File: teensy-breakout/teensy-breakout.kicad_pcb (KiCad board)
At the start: 6 copper layers, 240.5 x 168.5 mm, 82 parts, among them J1 USB_B, J10 1988820, J11 1988817, J12 1988817, J13 1988817, J14 1988817, J15 1988820, J17 1988956, J18 1988817, J19 1989010, J2 1988820, J20 1989010, J21 1988956, J22 1988817, J3 1988820, J4 1988820, J5 1988820, J6 1988820, J7 1988820, J8 1988833, J9 1988956, Q1 IRL530NSTRLPBF, SW1 7101MD9AQE, U1 Teensy4.1, U10 LSF0102DCUR, U3 FT232RL, U6 ICL7667CBAZA-TDKR, U7 LSF0102DCUR, U8 LSF0102DCUR

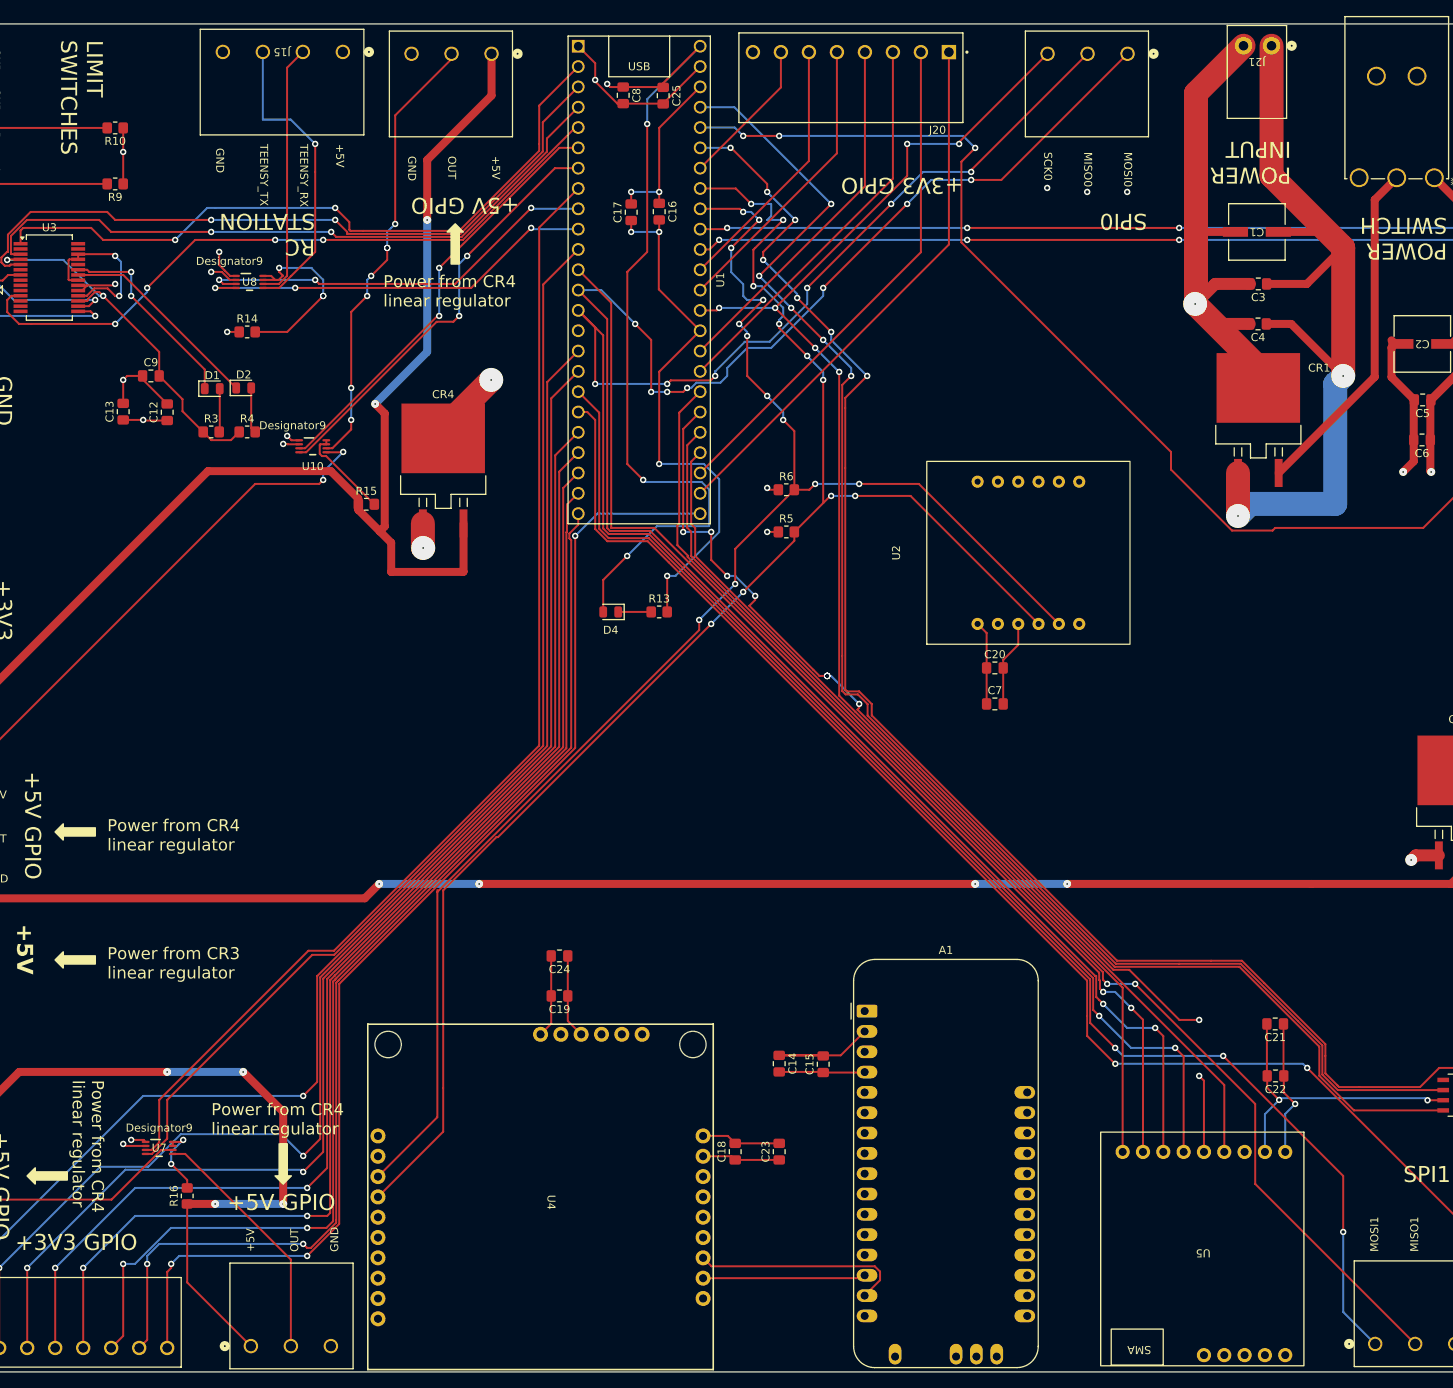
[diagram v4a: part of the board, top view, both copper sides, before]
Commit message: Added connection for limit switches, started work on adding headers
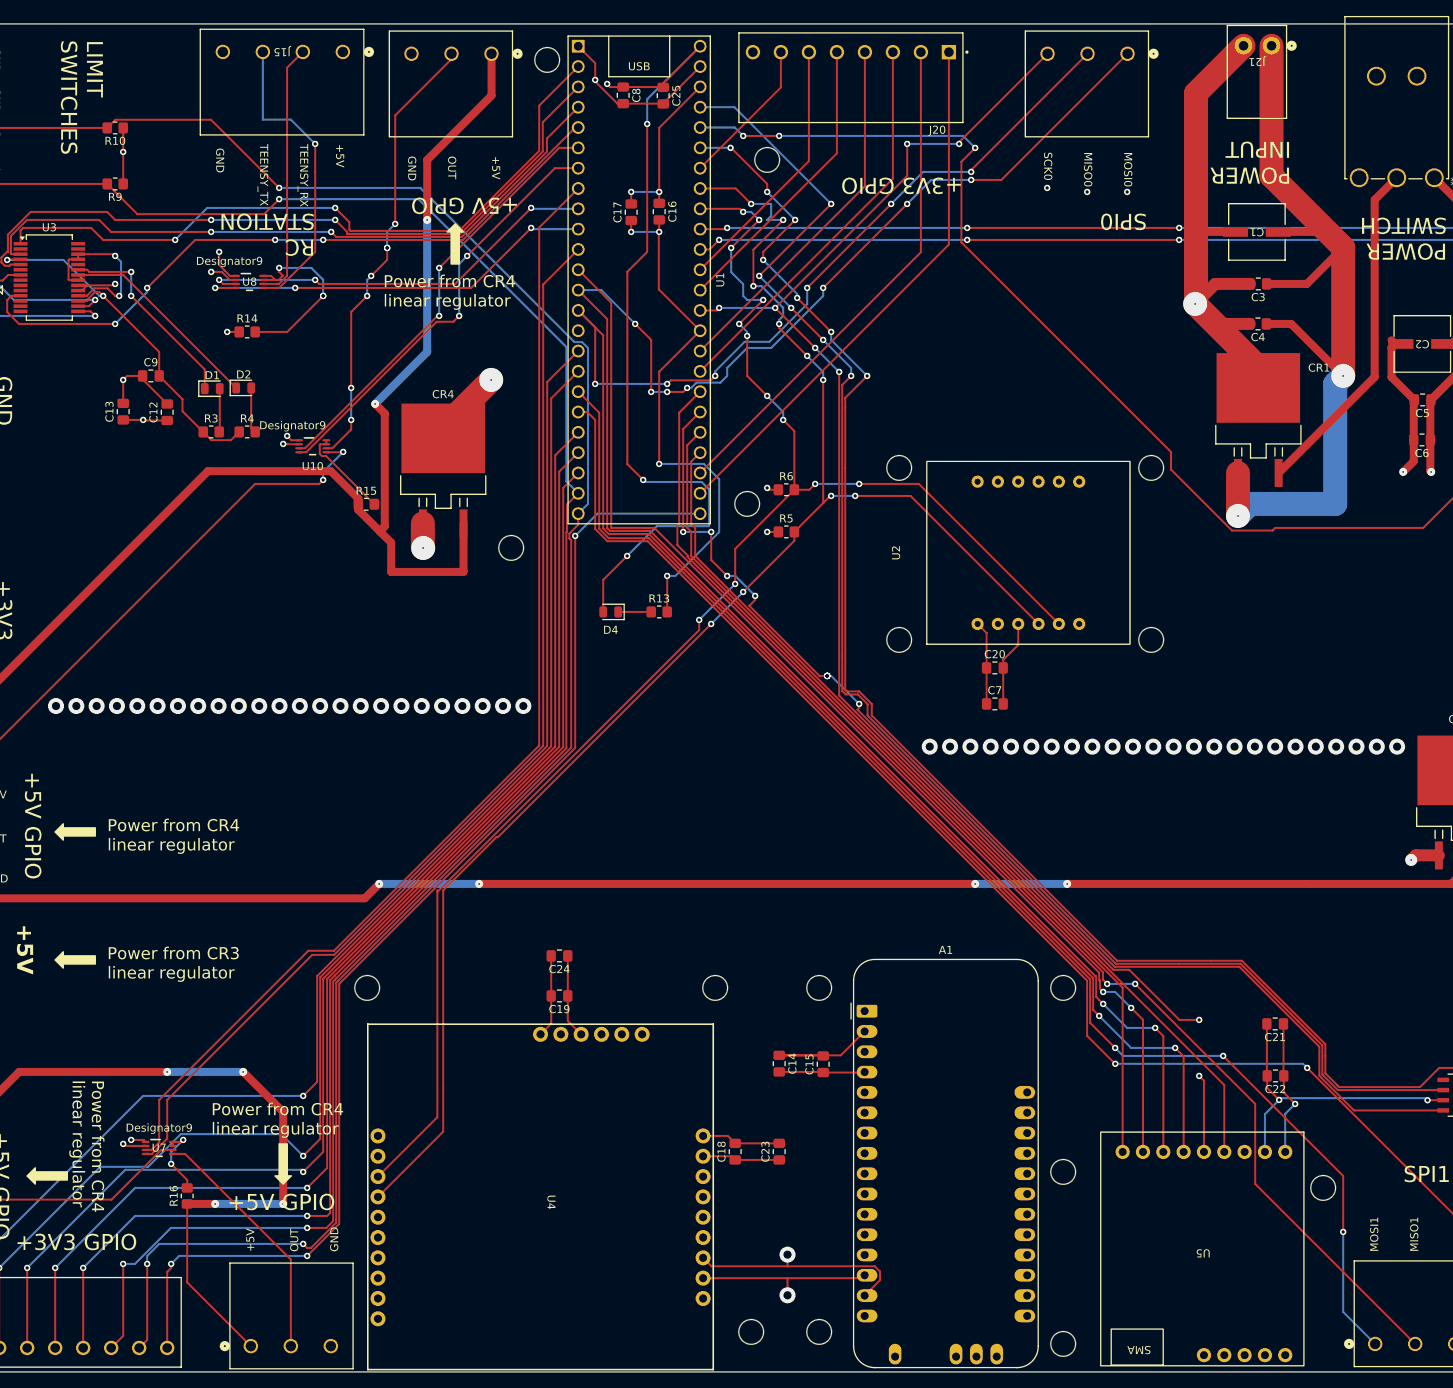
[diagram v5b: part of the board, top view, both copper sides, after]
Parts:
- added ?: , clipboard:fe42560d-e869-41d1-821b-38ac966b38b9, F.Cu at (164.0, 147.0)
- added ?: , clipboard:fe42560d-e869-41d1-821b-38ac966b38b9, F.Cu at (124.5, 86.5)
- added ?: , clipboard:fe42560d-e869-41d1-821b-38ac966b38b9, F.Cu at (133.5, 190.0)
- added ?: , clipboard:fe42560d-e869-41d1-821b-38ac966b38b9, F.Cu at (133.5, 147.0)
- added ?: , clipboard:fe42560d-e869-41d1-821b-38ac966b38b9, F.Cu at (99.5, 31.0)
- added ?: , clipboard:fe42560d-e869-41d1-821b-38ac966b38b9, F.Cu at (125.0, 190.0)
- added ?: , clipboard:fe42560d-e869-41d1-821b-38ac966b38b9, F.Cu at (164.0, 191.5)
- added ?: , clipboard:fe42560d-e869-41d1-821b-38ac966b38b9, F.Cu at (77.0, 147.0)
- added ?: , clipboard:fe42560d-e869-41d1-821b-38ac966b38b9, F.Cu at (143.5, 103.5)
- added ?: , clipboard:fe42560d-e869-41d1-821b-38ac966b38b9, F.Cu at (143.5, 82.0)
- added ?: , clipboard:fe42560d-e869-41d1-821b-38ac966b38b9, F.Cu at (175.0, 103.5)
- added ?: , clipboard:fe42560d-e869-41d1-821b-38ac966b38b9, F.Cu at (196.5, 172.0)
- added ?: , clipboard:fe42560d-e869-41d1-821b-38ac966b38b9, F.Cu at (164.0, 170.0)
- added ?: , clipboard:fe42560d-e869-41d1-821b-38ac966b38b9, F.Cu at (95.0, 92.0)
- added ?: , clipboard:fe42560d-e869-41d1-821b-38ac966b38b9, F.Cu at (175.0, 82.0)
- added ?: , clipboard:fe42560d-e869-41d1-821b-38ac966b38b9, F.Cu at (120.5, 147.0)
- added ?: , clipboard:fe42560d-e869-41d1-821b-38ac966b38b9, F.Cu at (127.0, 43.5)
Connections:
- J9 pad 1: GND -> Net-(D3-K)
- J9 pad 2: led_pos -> +12V
- R8 pad 2: led_pos -> Net-(D3-A)
- U1 pad 23: /J0_6 -> /LIM_L
- U1 pad 24: /J0_7 -> /LIM_R
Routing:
- net GND: track 338.7 -> 657.4 mm, vias 18 -> 21
- net +3V3: track 166.8 -> 345.5 mm, vias 11 -> 13
- net +5V: track 178.8 -> 309.3 mm, vias 9 -> 10
- net /PUL: track 190.0 -> 307.1 mm, vias 5 -> 6
- net /BRAKE: track 138.5 -> 252.3 mm, vias 3 -> 4
- net /ALM: track 228.3 -> 340.0 mm, vias 7 -> 8
- net /UART1 RX: track 87.4 -> 196.0 mm, vias 2 -> 3
- net /J1_7: track 18.7 -> 126.7 mm, vias 0 -> 1
- net /I2C0_SCL: track 199.3 -> 305.6 mm, vias 10 -> 11
- net /UART1 TX: track 90.0 -> 196.3 mm, vias 2 -> 3
- net /UART1 RTS: track 83.7 -> 186.8 mm, vias 2 -> 3
- net /I2C0_SDA: track 198.3 -> 300.4 mm, vias 12 -> 13
- net /UART1 CTS: track 85.8 -> 185.8 mm, vias 4 -> 5
- net Net-(U1-17_A3_TX4_SDA1): track 141.0 -> 238.0 mm, vias 4 -> 5
- net Net-(U1-16_A2_RX4_SCL1): track 148.5 -> 242.8 mm, vias 4 -> 5
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
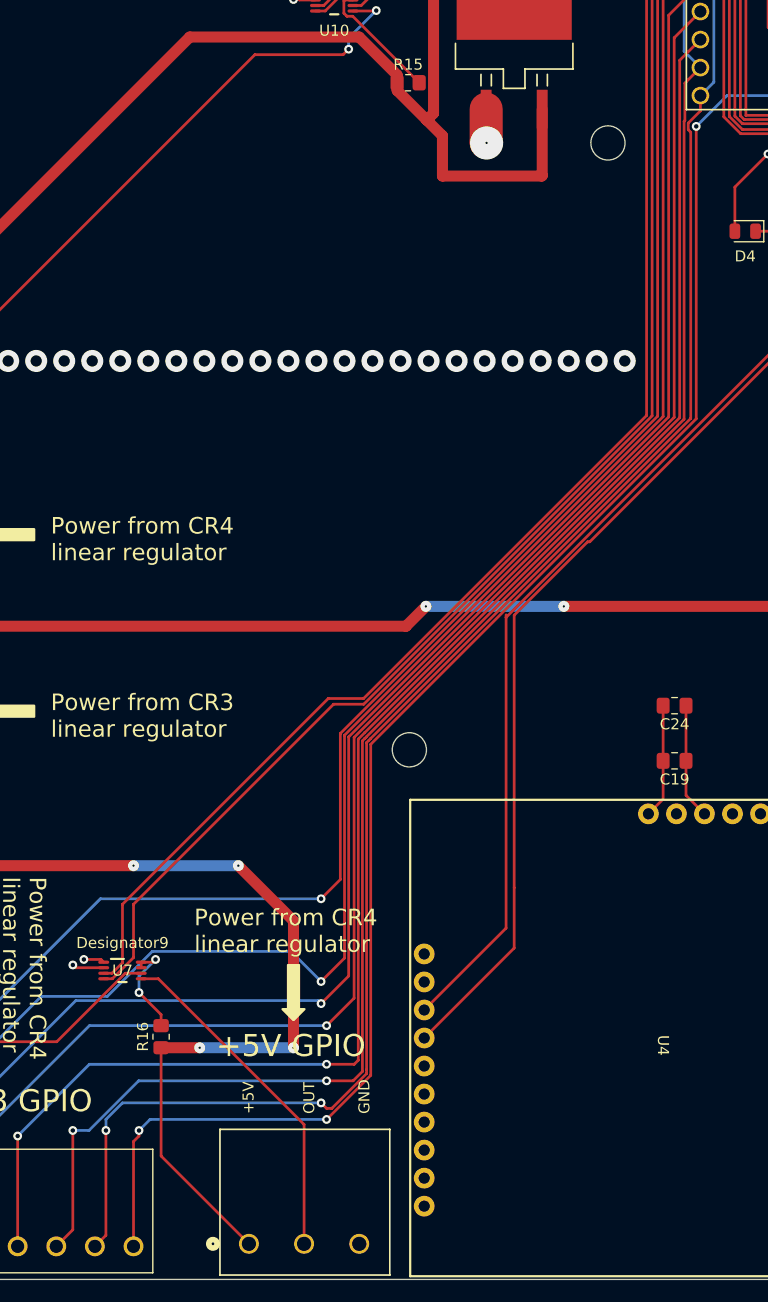
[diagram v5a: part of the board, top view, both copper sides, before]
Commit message: Fixed limit switch connection
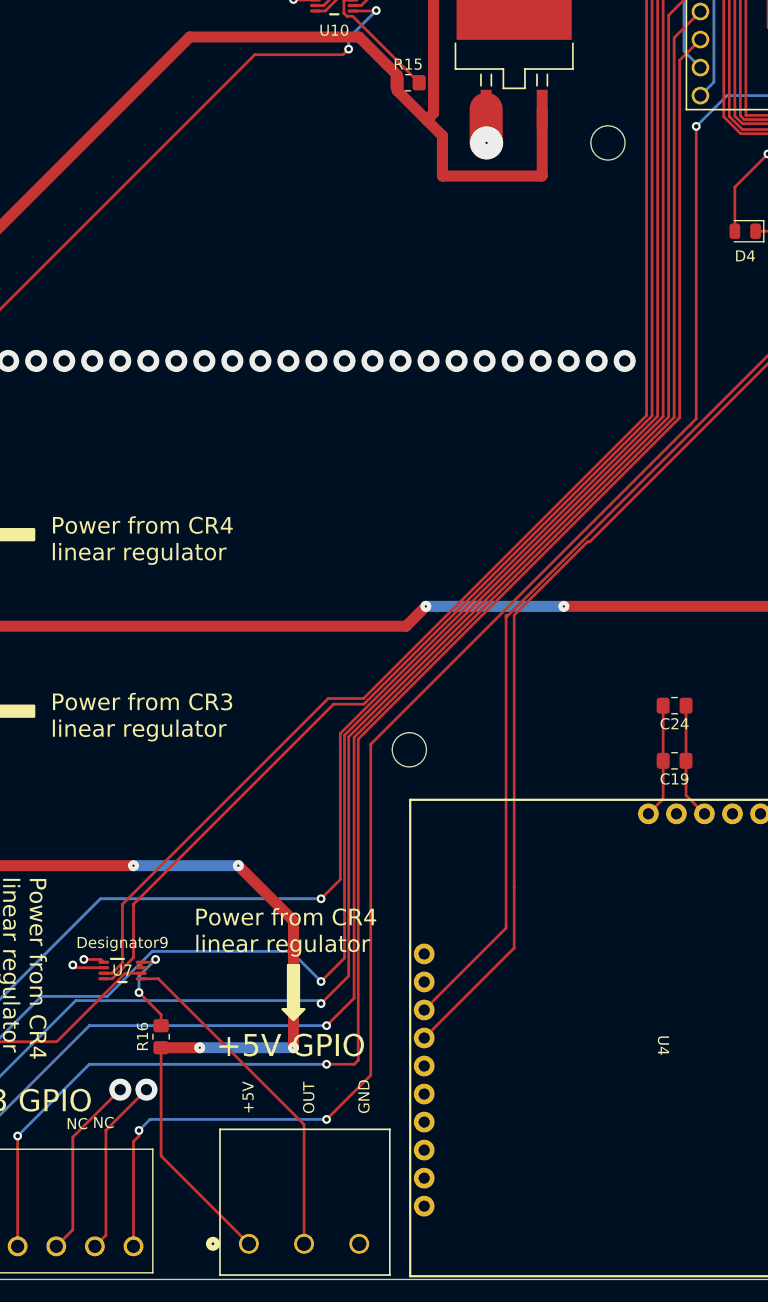
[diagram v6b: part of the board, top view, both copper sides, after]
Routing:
- net /J0_6: track 173.7 -> 16.6 mm, vias 3 -> 1
- net /J0_7: track 165.9 -> 16.1 mm, vias 3 -> 1
- net /LIM_L: track 114.5 -> 145.0 mm, vias 1 -> 2
- net /LIM_R: track 121.7 -> 148.6 mm, vias 1 -> 2
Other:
- board text added: "NC"

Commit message: Final commit before meeting
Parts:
- added REF**: PinHeader_1x06_P2.54mm_Vertical, Connector_PinHeader_2.54mm:PinHeader_1x06_P2.54mm_Vertical, F.Cu at (171.4, 140.7)
- added REF**: PinHeader_1x02_P2.54mm_Vertical, Connector_PinHeader_2.54mm:PinHeader_1x02_P2.54mm_Vertical, F.Cu at (144.3, 72.7)
- moved ? 163.6 mm to (196.5, 191.6)
- moved SW1 1.17 mm to (210.4, 46.9)
- moved J9 0.50 mm to (250.8, 44.1)
- moved J6 0.48 mm to (250.8, 78.8)
- moved J2 0.43 mm to (250.8, 55.7)
- moved J4 0.37 mm to (250.9, 103.7)
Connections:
- J9 pad 2: +12V -> Net-(D3-A)
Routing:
- net GND: track 657.4 -> 737.3 mm, vias 21 -> 22
- net Net-(D3-K): track 79.7 -> 123.9 mm, vias 0 -> 4
- net /RF_G0: track 171.5 -> 199.0 mm
- net /RF_RST: track 171.6 -> 198.4 mm
- net /RF_CS: track 214.2 -> 241.0 mm
- net /MOSI0: track 307.2 -> 334.0 mm
- net /MISO0: track 295.9 -> 322.7 mm
- net Net-(D3-A): track 5.89 -> 27.7 mm
- net (no net): track 21.8 -> 0.00 mm, vias 3 -> 0
- net /I2C0_SCL: track 305.6 -> 321.2 mm
- net /I2C0_SDA: track 300.4 -> 315.2 mm
- net /SCK0: track 276.6 -> 287.2 mm
- net +5V: track 309.3 -> 313.5 mm
- net Net-(CR1-OUTPUT): track 43.0 -> 46.4 mm
- net /J0_4: track 189.3 -> 190.4 mm
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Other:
- board text added: "11"
- board text added: "12"
- board text added: "13"
- board text added: "16"
- board text added: "17"
- board text added: "21"
- board text added: "23"
- board text added: "24"
- board text added: "25"
- board text added: "26"
- board text added: "27"
- board text added: "28"
- board text added: "29"
- board text added: "30"
- board text added: "31"
- board text added: "32"
- board text added: "33"
- board text added: "38"
- board text added: "39"
- board text added: "4"
- board text added: "5"
- board text added: "6"
- board text added: "7"
- board text added: "8"
- board text added: "Bank 0"
- board text added: "Bank 1"
- board text added: "I2C0"
- board text added: "SCL"
- board text added: "SDA"
